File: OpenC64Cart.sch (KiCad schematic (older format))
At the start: 10 parts, among them P1 CONN_01X03, P2 CONN_01X02, P3 CONN_01X02, P4 CONN_01X03, P5 CONN_01X03, P6 CONN_01X03, SW1 RESET_SW, U1 C64-Exp-Port, U2 27512

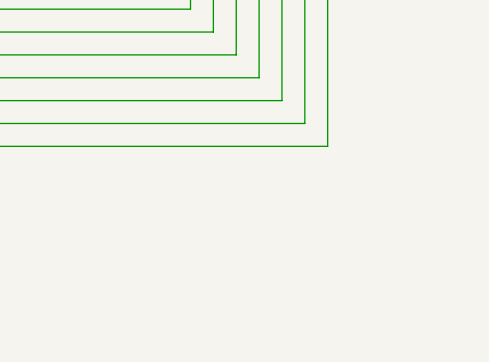
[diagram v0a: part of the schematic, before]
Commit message: Use SMD/THT combo footprint for cap, make peg hole 0.5mm bigger, fix parts for latest Kicad Thanks bigby for the peg hole size hint!
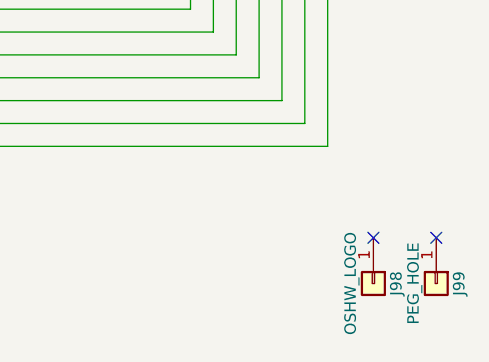
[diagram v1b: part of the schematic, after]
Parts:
- added J98: OSHW_LOGO, w_logo:Logo_copper_OSHW_12x13mm, symbol Conn_01x01
- added J99: PEG_HOLE, Connectors:1pin, symbol Conn_01x01
- C1: footprint smd_cap:c_0805 -> OpenC64Cart:C_0805+THT
- P1, P4, P5, P6: footprint Pin_Headers:Pin_Header_Straight_1x03 -> OpenC64Cart:Pin_Header_Straight_1x03-NoSilkS
- P2, P3: footprint Pin_Headers:Pin_Header_Straight_1x02 -> OpenC64Cart:Pin_Header_Straight_1x02-NoSilkS
- SW1: footprint w_switch:PCB_PUSH -> OpenC64Cart:PCB_PUSH
- U1: footprint Sukko:C64-Cart -> OpenC64Cart:C64-Cart
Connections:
- no-connect marks 12 -> 14
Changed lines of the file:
@@
 Sheet 1 1
 Title "C64 8K Lo/Hi-Rom Cartridge"
-Date "2017-07-21"
-Rev ""
+Date "2017-12-30"
+Rev "V2"
 Comp "SukkoPera"
 Comment1 "Thanks to http://blog.worldofjani.com/?p=879"
@@
 F 0 "U1" H 4100 3850 50  0000 C CNN
 F 1 "C64-Exp-Port" H 4100 5250 50  0000 C CNN
-F 2 "Sukko:C64-Cart" H 4100 3950 50  0001 C CNN
+F 2 "OpenC64Cart:C64-Cart" H 4100 3950 50  0001 C CNN
 F 3 "https://www.c64-wiki.com/wiki/Expansion_Port" H 4100 3950 50  0001 C CNN
 	1    4100 3950
@@
 F 0 "C1" H 9125 1650 50  0000 L CNN
 F 1 "C" H 9125 1450 50  0000 L CNN
-F 2 "smd_cap:c_0805" H 9138 1400 50  0001 C CNN
+F 2 "OpenC64Cart:C_0805+THT" H 9138 1400 50  0001 C CNN
 F 3 "" H 9100 1550 50  0000 C CNN
 	1    9100 1550
@@
 F 0 "P2" H 5200 4650 50  0000 C CNN
 F 1 "CONN_01X02" V 5300 4500 50  0001 C CNN
-F 2 "Pin_Headers:Pin_Header_Straight_1x02" H 5200 4500 50  0001 C CNN
+F 2 "OpenC64Cart:Pin_Header_Straight_1x02-NoSilkS" H 5200 4500 50  0001 C CNN
 F 3 "" H 5200 4500 50  0000 C CNN
 	1    5200 4500
@@
 F 0 "P3" H 5600 4550 50  0000 C CNN
 F 1 "CONN_01X02" V 5700 4400 50  0001 C CNN
-F 2 "Pin_Headers:Pin_Header_Straight_1x02" H 5600 4400 50  0001 C CNN
+F 2 "OpenC64Cart:Pin_Header_Straight_1x02-NoSilkS" H 5600 4400 50  0001 C CNN
 F 3 "" H 5600 4400 50  0000 C CNN
 	1    5600 4400
@@
 F 0 "P1" H 4100 6200 50  0000 C CNN
 F 1 "CONN_01X03" V 4200 6000 50  0001 C CNN
-F 2 "Pin_Headers:Pin_Header_Straight_1x03" H 4100 6000 50  0001 C CNN
+F 2 "OpenC64Cart:Pin_Header_Straight_1x03-NoSilkS" H 4100 6000 50  0001 C CNN
 F 3 "" H 4100 6000 50  0000 C CNN
 	1    4100 6000
@@
 F 0 "SW1" H 2250 5050 50  0000 C CNN
 F 1 "RESET_SW" H 2250 4650 50  0000 C CNN
-F 2 "w_switch:PCB_PUSH" H 2250 4800 50  0001 C CNN
+F 2 "OpenC64Cart:PCB_PUSH" H 2250 4800 50  0001 C CNN
 F 3 "" H 2250 4800 50  0000 C CNN
 	1    2250 4800
@@
 F 0 "P4" H 6850 4750 50  0000 C CNN
 F 1 "CONN_01X03" V 6950 4550 50  0001 C CNN
-F 2 "Pin_Headers:Pin_Header_Straight_1x03" H 6850 4550 50  0001 C CNN
+F 2 "OpenC64Cart:Pin_Header_Straight_1x03-NoSilkS" H 6850 4550 50  0001 C CNN
 F 3 "" H 6850 4550 50  0000 C CNN
 	1    6850 4550
@@
 F 0 "P5" H 7300 4750 50  0000 C CNN
 F 1 "CONN_01X03" V 7400 4550 50  0001 C CNN
-F 2 "Pin_Headers:Pin_Header_Straight_1x03" H 7300 4550 50  0001 C CNN
+F 2 "OpenC64Cart:Pin_Header_Straight_1x03-NoSilkS" H 7300 4550 50  0001 C CNN
 F 3 "" H 7300 4550 50  0000 C CNN
 	1    7300 4550
@@
 F 0 "P6" H 7700 4750 50  0000 C CNN
 F 1 "CONN_01X03" V 7800 4550 50  0001 C CNN
-F 2 "Pin_Headers:Pin_Header_Straight_1x03" H 7700 4550 50  0001 C CNN
+F 2 "OpenC64Cart:Pin_Header_Straight_1x03-NoSilkS" H 7700 4550 50  0001 C CNN
 F 3 "" H 7700 4550 50  0000 C CNN
 	1    7700 4550
@@
 	7050 4350 7100 4350
 Connection ~ 7050 4350
+$Comp
+L Conn_01x01 J99
+U 1 1 5A47B067
+P 11025 6250
+F 0 "J99" H 11025 6350 50  0000 C CNN
+F 1 "PEG_HOLE" H 11025 6150 50  0000 C CNN
+F 2 "Connectors:1pin" H 11025 6250 50  0001 C CNN
+F 3 "" H 11025 6250 50  0001 C CNN
+	1    11025 6250
+	0    1    1    0
+$EndComp
+$Comp
+L Conn_01x01 J98
+U 1 1 5A47B1EF
+P 10750 6250
+F 0 "J98" H 10750 6350 50  0000 C CNN
+F 1 "OSHW_LOGO" H 10750 6150 50  0000 C CNN
+F 2 "w_logo:Logo_copper_OSHW_12x13mm" H 10750 6250 50  0001 C CNN
+F 3 "" H 10750 6250 50  0001 C CNN
+	1    10750 6250
+	0    1    1    0
+$EndComp
+NoConn ~ 10750 6050
+NoConn ~ 11025 6050
 $EndSCHEMATC

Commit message: More final touches
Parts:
- C1: value C -> 100n
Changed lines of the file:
@@
 P 9100 1550
 F 0 "C1" H 9125 1650 50  0000 L CNN
-F 1 "C" H 9125 1450 50  0000 L CNN
+F 1 "100n" H 9125 1450 50  0000 L CNN
 F 2 "OpenC64Cart:C_0805+THT" H 9138 1400 50  0001 C CNN
 F 3 "" H 9100 1550 50  0000 C CNN

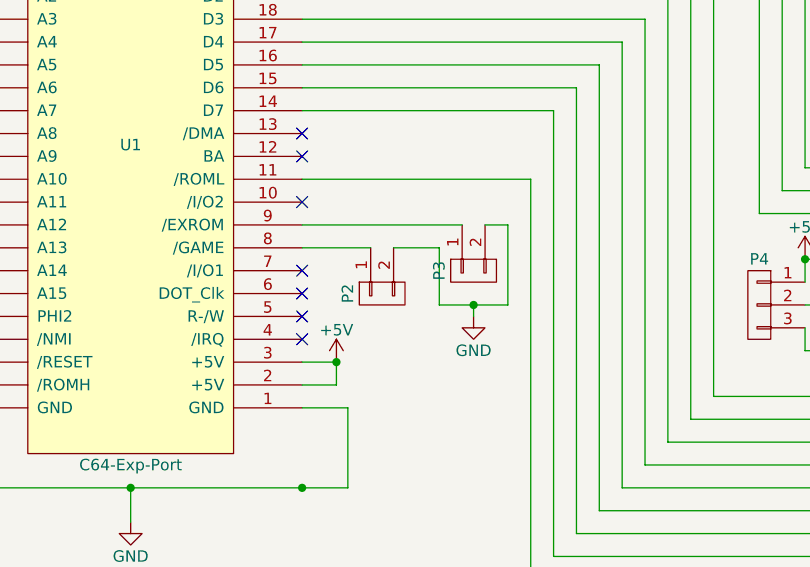
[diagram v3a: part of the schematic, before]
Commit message: Use a single jumper for GAME/EXROM
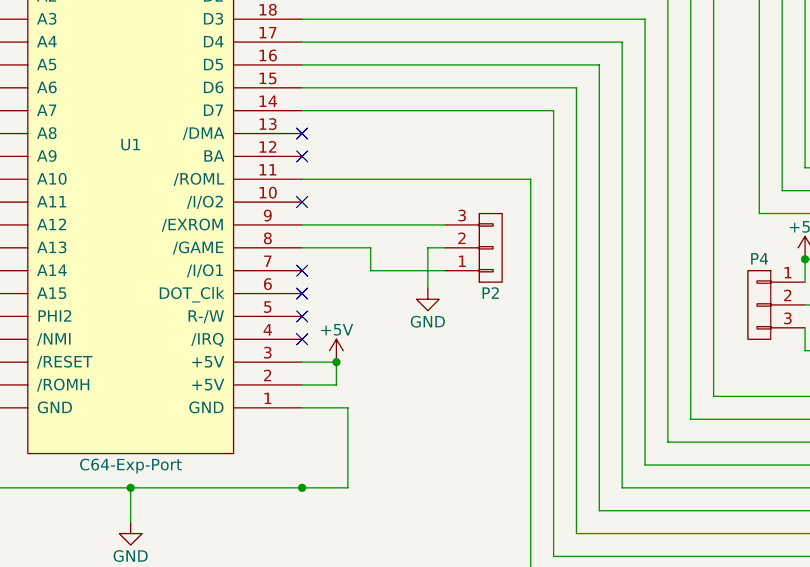
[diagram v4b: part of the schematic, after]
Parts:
- removed P2, P3: CONN_01X02, OpenC64Cart:Pin_Header_Straight_1x02-NoSilkS, symbol CONN_01X02
- added P2: CONN_01X03, OpenC64Cart:Pin_Header_Straight_1x03-NoSilkS, symbol CONN_01X03
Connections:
- net GND: now also P2.2 (P2)
- net at U1.8 (/GAME): now also P2.1 (P1)
- net at U1.9 (/EXROM): now also P2.3 (P3)
